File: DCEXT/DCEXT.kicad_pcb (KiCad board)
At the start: 2 copper layers, 77 x 100.7 mm, 13 parts, among them J3 USB1015-XX-X-X_REVC, J4 USB1015-XX-X-X_REVC, J6 Conn_02x25_Odd_Even, Q1 SI2310, U1 MPCIE-DevTerm, U2 USBUF02W6, U3 USBUF02W6, U4 SY6280

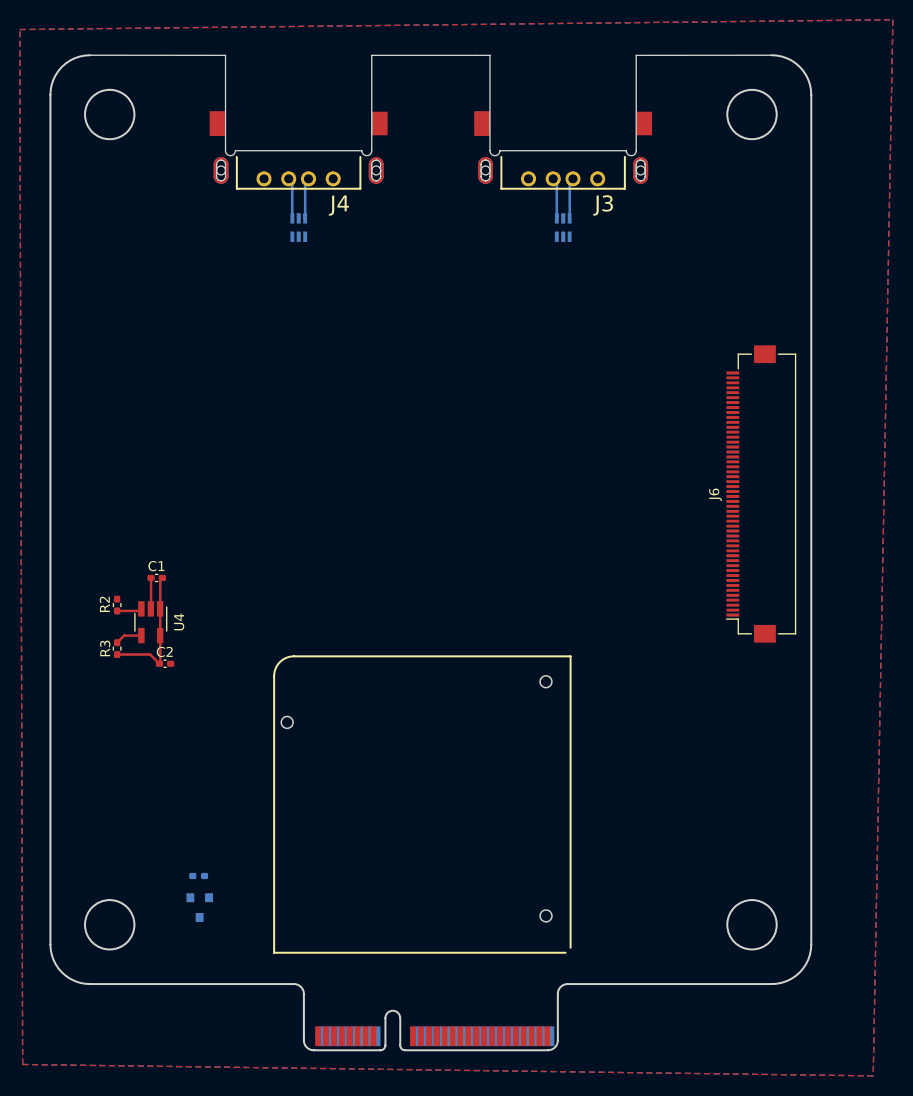
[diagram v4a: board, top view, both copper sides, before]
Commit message: Fix usb position (for the last time !), speaker connector and routing
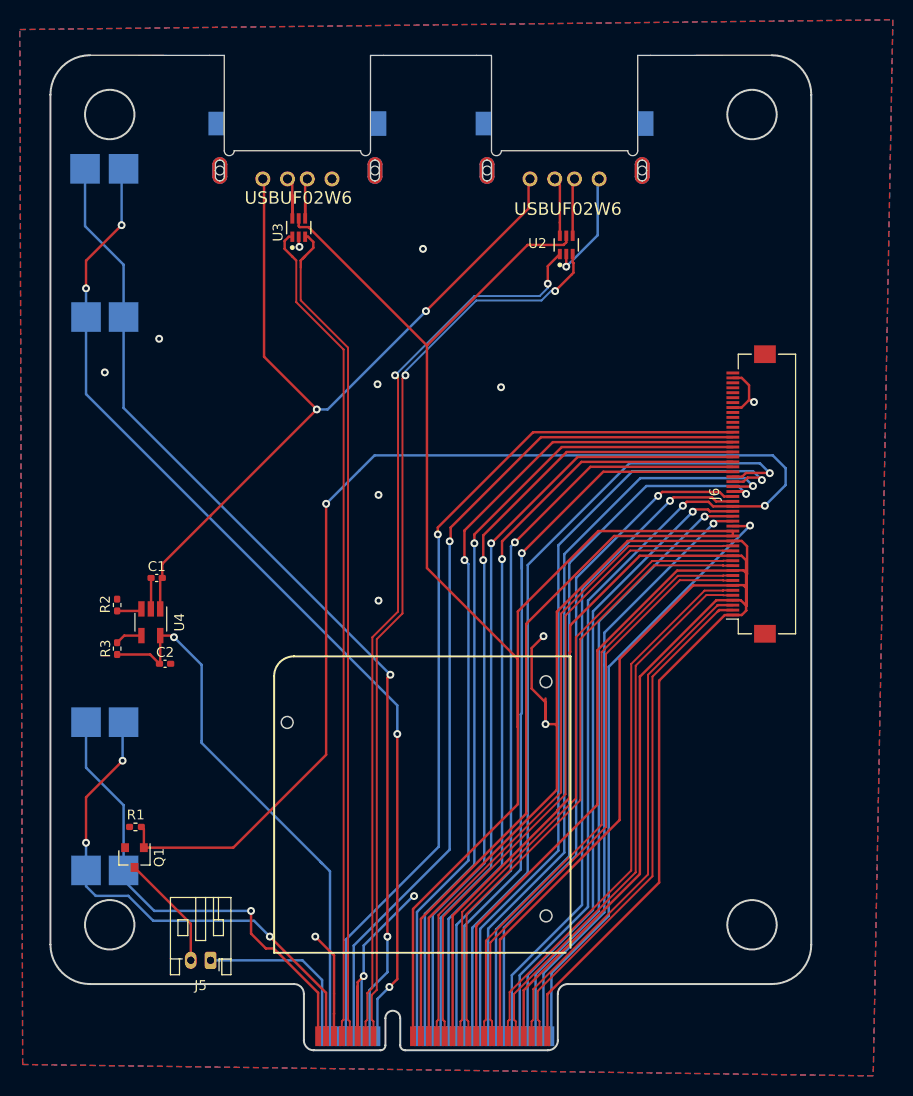
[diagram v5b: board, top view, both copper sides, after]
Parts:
- added J5: FAN_CON, Connector_JST:JST_PH_S2B-PH-K_1x02_P2.00mm_Horizontal, F.Cu at (75.2, 133.4)
- added TP1: TestPoint, TestPoint:TestPoint_Pad_3.0x3.0mm, B.Cu at (66.4, 124.3)
- added TP2: TestPoint, TestPoint:TestPoint_Pad_3.0x3.0mm, B.Cu at (66.4, 109.3)
- added TP3: TestPoint, TestPoint:TestPoint_Pad_3.0x3.0mm, B.Cu at (62.6, 109.3)
- added TP4: TestPoint, TestPoint:TestPoint_Pad_3.0x3.0mm, B.Cu at (62.6, 124.3)
- added TP5: TestPoint, TestPoint:TestPoint_Pad_3.0x3.0mm, B.Cu at (66.4, 68.3)
- added TP6: TestPoint, TestPoint:TestPoint_Pad_3.0x3.0mm, B.Cu at (62.6, 68.3)
- added TP7: TestPoint, TestPoint:TestPoint_Pad_3.0x3.0mm, B.Cu at (62.5, 53.3)
- added TP8: TestPoint, TestPoint:TestPoint_Pad_3.0x3.0mm, B.Cu at (66.4, 53.3)
- J3, J4: moved to B.Cu
- Q1: value SI2310 -> BSS138; moved to F.Cu
- R1, U2, U3: moved to F.Cu
- moved Q1 8.32 mm to (67.5, 123.0)
- moved R1 8.10 mm to (67.6, 119.9), turned to 180 degrees
- moved U2 1.78 mm to (111.2, 61.0)
- moved J3 0.15 mm to (111.0, 48.3), turned to 0 degrees
- moved J4 0.12 mm to (84.0, 48.3), turned to 0 degrees
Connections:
- C1 pad 2: +5V -> /USB_5V
- J6 pad 1: /GPIO34 -> GND
- J6 pad 10: /GPIO41 -> GND
- J6 pad 11: /GPIO29 -> /CAM1_D2_N
- J6 pad 12: /GPIO40 -> /CAM1_D2_P
- J6 pad 13: /GPIO28 -> GND
- J6 pad 14: /GPIO39 -> /CAM1_D3_N
- J6 pad 15: +3V3 -> /CAM1_D3_P
- J6 pad 16: /GPIO38 -> GND
- J6 pad 17: +5V -> +3V3
- J6 pad 18: /GPIO37 -> +3V3
- J6 pad 19: GND -> /GPIO45
- J6 pad 2: /GPIO45 -> /CAM1_D0_N
- J6 pad 20: /GPIO36 -> /GPIO44
- J6 pad 21: /CAM1_D0_N -> /GPIO43
- J6 pad 22: /GPIO35 -> /GPIO42
- J6 pad 23: /CAM1_D0_P -> /GPIO41
- J6 pad 24: +3V3 -> /GPIO40
- J6 pad 25: GND -> /GPIO39
- J6 pad 26: +5V -> /GPIO38
- J6 pad 27: /CAM1_D1_N -> /GPIO37
- J6 pad 28: /UART_RX -> /GPIO36
- J6 pad 29: /CAM1_D1_P -> /GPIO35
- J6 pad 3: /GPIO33 -> /CAM1_D0_P
- J6 pad 30: /UART_TX -> /GPIO34
- J6 pad 31: GND -> /GPIO33
- J6 pad 32: Net-(J6-Pad32) -> /GPIO32
- J6 pad 33: /CAM1_C_N -> /GPIO31
- J6 pad 34: Net-(J6-Pad34) -> /GPIO30
- J6 pad 35: /CAM1_C_P -> /GPIO29
- J6 pad 36: Net-(J6-Pad36) -> /GPIO28
- J6 pad 37: GND -> +5V
- J6 pad 38: Net-(J6-Pad38) -> +5V
- J6 pad 39: /CAM1_D2_N -> Net-(J6-Pad39)
- J6 pad 4: /GPIO44 -> GND
- J6 pad 41: /CAM1_D2_P -> Net-(J6-Pad41)
- J6 pad 45: /CAM1_D3_N -> Net-(J6-Pad45)
- J6 pad 47: /CAM1_D3_P -> Net-(J6-Pad47)
- J6 pad 5: /GPIO32 -> /CAM1_D1_N
- J6 pad 6: /GPIO43 -> /CAM1_D1_P
- J6 pad 7: /GPIO31 -> GND
- J6 pad 8: /GPIO42 -> /CAM1_C_N
- J6 pad 9: /GPIO30 -> /CAM1_C_P
- Q1 pad 1: Net-(Q1-Pad1) -> /GPIO41
- R1 pad 1: Net-(Q1-Pad1) -> /GPIO41
- U4 pad 1: +5V -> /USB_5V
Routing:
- net GND: track 3.15 -> 454.0 mm, vias 0 -> 15
- net +5V: track 13.5 -> 254.3 mm, vias 0 -> 3
- net +3V3: track 0.00 -> 224.0 mm
- net /GPIO41: track 0.00 -> 172.9 mm, vias 0 -> 3
- net /SPK_RN: track 0.00 -> 103.2 mm, vias 0 -> 4
- net /SPK_RP: track 0.00 -> 101.5 mm, vias 0 -> 2
- net /USB4_D_P: track 0.00 -> 91.8 mm, vias 0 -> 2
- net /USB4_D_N: track 0.00 -> 91.4 mm, vias 0 -> 2
- net /USB_5V: track 0.00 -> 85.2 mm, vias 0 -> 2
- net /GPIO28: track 0.00 -> 84.4 mm, vias 0 -> 1
- net /USB3_D_P: track 0.00 -> 84.3 mm
- net /USB3_D_N: track 0.00 -> 84.0 mm
- net /GPIO35: track 0.00 -> 83.1 mm, vias 0 -> 1
- net /GPIO29: track 0.00 -> 82.7 mm, vias 0 -> 1
- net /GPIO30: track 0.00 -> 81.6 mm, vias 0 -> 1
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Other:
- outline, holes or cut-outs redrawn
- board text added: "1.0 mm PCB"
- board text added: "Height limit inside box : 2 mm Height limit of the rest : 4.5 mm"

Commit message: Add USB hub, routing and start part sourcing
Spoiller alert : everything is out of stock ...
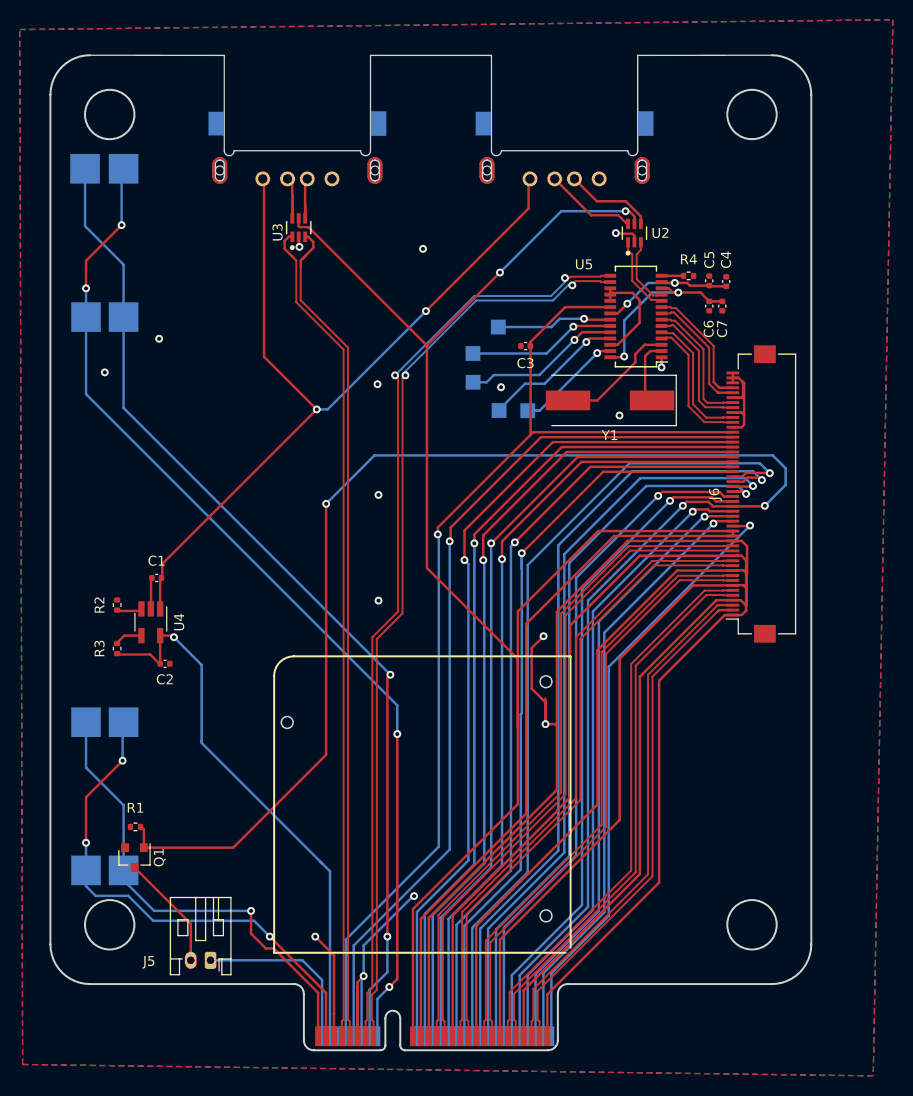
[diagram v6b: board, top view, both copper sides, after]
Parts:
- added C3: 10uF, Capacitor_SMD:C_0402_1005Metric, F.Cu at (107.1, 71.2)
- added C4: 10uF, Capacitor_SMD:C_0402_1005Metric, F.Cu at (127.4, 64.7)
- added C5: 0.1uF, Capacitor_SMD:C_0402_1005Metric, F.Cu at (125.7, 64.6)
- added C6: 10uF, Capacitor_SMD:C_0402_1005Metric, F.Cu at (125.7, 67.2)
- added C7: 0.1uF, Capacitor_SMD:C_0402_1005Metric, F.Cu at (127.0, 67.2)
- added R4: 2.7K, Resistor_SMD:R_0402_1005Metric, F.Cu at (123.6, 64.1)
- added TP10: TestPoint, TestPoint:TestPoint_Pad_1.5x1.5mm, B.Cu at (101.8, 72.0)
- added TP11: TestPoint, TestPoint:TestPoint_Pad_1.5x1.5mm, B.Cu at (101.8, 74.9)
- added TP12: TestPoint, TestPoint:TestPoint_Pad_1.5x1.5mm, B.Cu at (104.3, 69.3)
- added TP13: TestPoint, TestPoint:TestPoint_Pad_1.5x1.5mm, B.Cu at (104.4, 77.8)
- added TP9: TestPoint, TestPoint:TestPoint_Pad_1.5x1.5mm, B.Cu at (107.3, 77.8)
- added U5: FE1.1s, Package_SO:SSOP-28_3.9x9.9mm_P0.635mm, F.Cu at (118.2, 68.2)
- added Y1: 12Mhz 49MD-12.00-20-10-10/A, Crystal:Crystal_SMD_HC49-SD, F.Cu at (115.6, 76.7)
- C1, C2: footprint Capacitor_SMD:C_0402_1005Metric_Pad0.74x0.62mm_HandSolder -> Capacitor_SMD:C_0402_1005Metric
- R1, R2, R3: footprint Resistor_SMD:R_0402_1005Metric_Pad0.72x0.64mm_HandSolder -> Resistor_SMD:R_0402_1005Metric
- moved U2 7.00 mm to (118.1, 59.8)
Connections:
- J6 pad 39: Net-(J6-Pad39) -> GND
- J6 pad 40: Net-(J6-Pad40) -> /USB6_D_N
- J6 pad 41: Net-(J6-Pad41) -> /USB6_D_P
- J6 pad 42: Net-(J6-Pad42) -> GND
- J6 pad 43: GND -> /USB7_D_N
- J6 pad 44: Net-(J6-Pad44) -> /USB7_D_P
- J6 pad 45: Net-(J6-Pad45) -> GND
- J6 pad 46: Net-(J6-Pad46) -> /USB8_D_N
- J6 pad 47: Net-(J6-Pad47) -> /USB8_D_P
- J6 pad 48: Net-(J6-Pad48) -> GND
- J6 pad 50: Net-(J6-Pad50) -> GND
- U2 pad 1: /USB4_D_N -> /USB5_D_N
- U2 pad 3: /USB4_D_P -> /USB5_D_P
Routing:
- net +5V: track 254.3 -> 273.2 mm
- net Net-(C6-Pad2): track 0.00 -> 18.4 mm, vias 0 -> 2
- net Net-(TP11-Pad1): track 0.00 -> 16.0 mm, vias 0 -> 1
- net Net-(TP10-Pad1): track 0.00 -> 15.2 mm, vias 0 -> 1
- net Net-(C4-Pad2): track 0.00 -> 14.5 mm, vias 0 -> 2
- net Net-(TP13-Pad1): track 0.00 -> 14.3 mm, vias 0 -> 1
- net /USB6_D_N: track 0.00 -> 13.8 mm
- net /USB6_D_P: track 0.00 -> 13.8 mm
- net /USB7_D_P: track 0.00 -> 13.7 mm
- net /USB7_D_N: track 0.00 -> 13.7 mm
- net /USB8_D_N: track 0.00 -> 12.8 mm
- net /USB8_D_P: track 0.00 -> 12.7 mm
- net Net-(U5-Pad3): track 0.00 -> 12.3 mm
- net Net-(TP9-Pad1): track 0.00 -> 12.0 mm, vias 0 -> 1
- net Net-(TP12-Pad1): track 0.00 -> 11.8 mm, vias 0 -> 1
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
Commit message: Change USB connector to something in stock :/ + gerber files
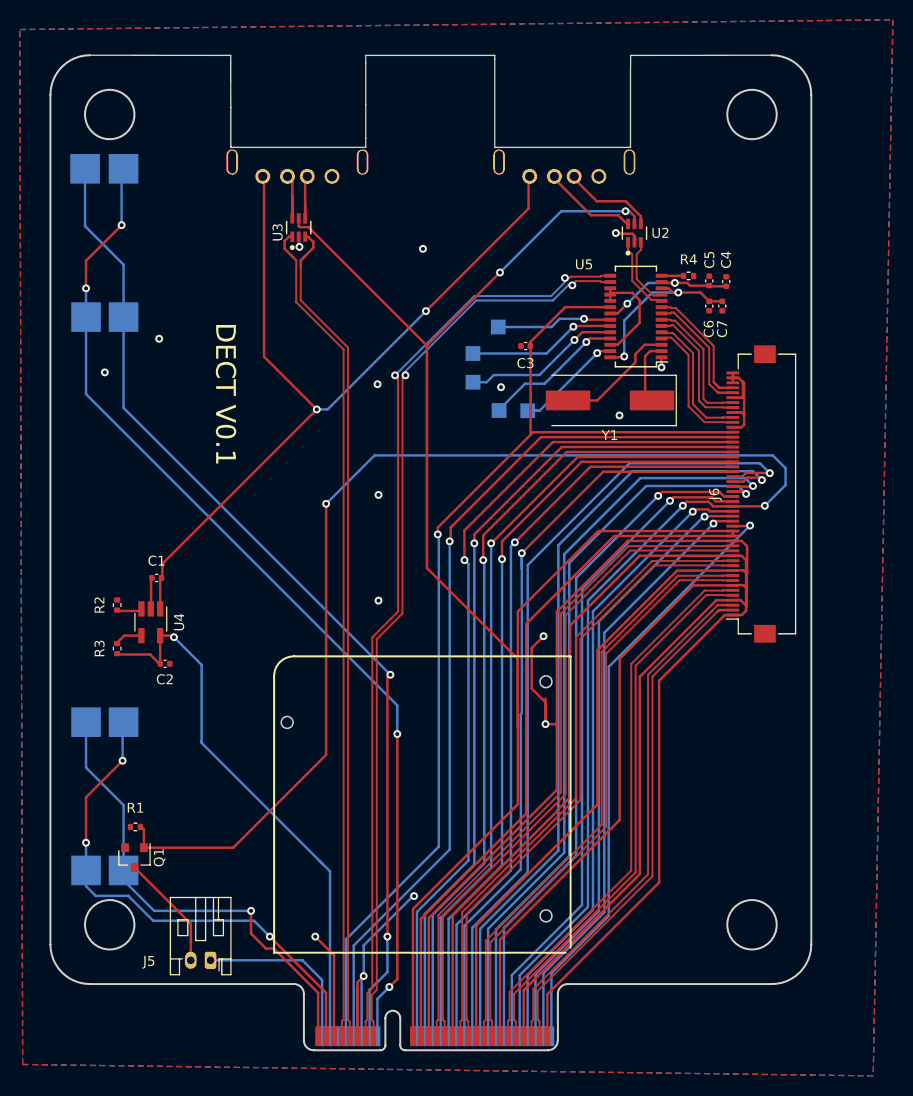
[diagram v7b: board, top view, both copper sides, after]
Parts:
- J3, J4: footprint DCEXT:GCT_USB1015-XX-X-X_REVC -> DCEXT:USB-A-TH_USB-M-55-F
- moved J3 5.02 mm to (111.0, 53.3)
- moved J4 5.02 mm to (84.0, 53.3)
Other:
- outline, holes or cut-outs redrawn
- board text added: "DECT V0.1"
